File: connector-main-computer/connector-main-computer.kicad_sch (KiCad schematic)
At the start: 38 parts, among them J1 DVI-I_Dual_Link, J10 Conn_01x04_MountingPin, J11 Conn_01x04_MountingPin, J12 Conn_01x02_MountingPin, J13 Conn_01x04_MountingPin, J2 Conn_01x03_MountingPin, J3 Conn_01x03_MountingPin, J4 Conn_01x03_MountingPin, J5 Conn_01x03_MountingPin, J6 Conn_01x03_MountingPin, J7 Conn_01x04_MountingPin, J8 Conn_01x04_MountingPin, J9 Conn_01x04_MountingPin, U1 INA199xxDCK, U2 INA199xxDCK, U3 P82B96, U4 SN65HVD11HD, U5 74AHCT1G04

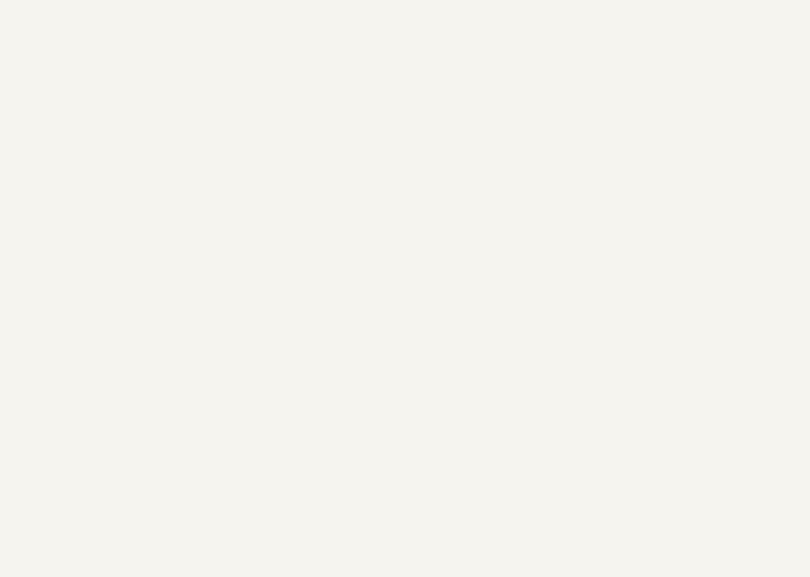
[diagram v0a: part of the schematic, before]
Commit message: Add first revision of board for main computer connector
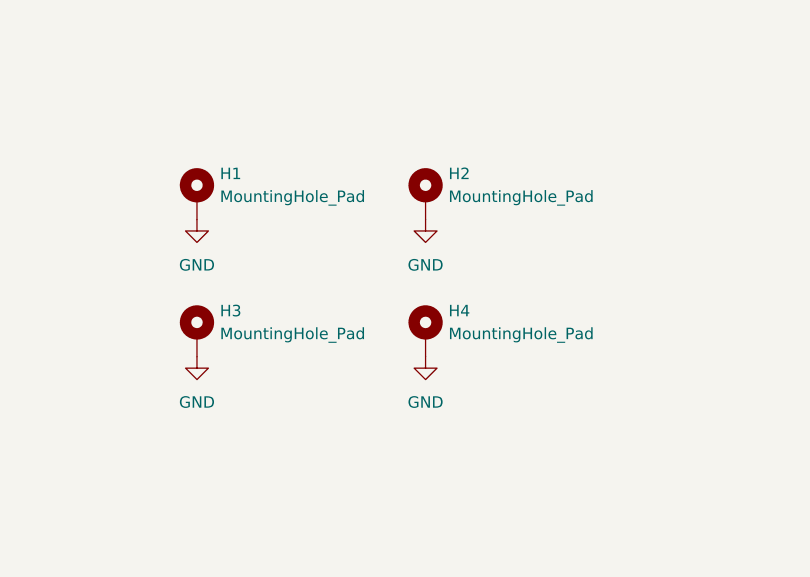
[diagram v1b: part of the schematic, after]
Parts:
- added H1, H2, H3, H4: MountingHole_Pad, MountingHole:MountingHole_3.2mm_M3_Pad_Via, symbol Mechanical:MountingHole_Pad
- C1, C2, C3, C4, C5: footprint (none) -> Capacitor_SMD:C_0805_2012Metric
- D3: footprint (none) -> Diode_SMD:D_MiniMELF
- FB1, FB2, FB3, FB4, FB5: footprint (none) -> Inductor_SMD:L_0805_2012Metric
- J1: footprint (none) -> Connector_Video:DVI-I_Molex_74320-1004_Horizontal
- J10, J11, J13, J7, J8, J9: footprint (none) -> Connector_JST:JST_PH_S4B-PH-SM4-TB_1x04-1MP_P2.00mm_Horizontal
- J12: footprint (none) -> Connector_JST:JST_PH_S2B-PH-SM4-TB_1x02-1MP_P2.00mm_Horizontal
- J2, J3, J4, J5, J6: footprint (none) -> Connector_JST:JST_PH_S3B-PH-SM4-TB_1x03-1MP_P2.00mm_Horizontal
- R1, R2, R5: footprint (none) -> Resistor_SMD:R_2512_6332Metric
- R3, R4, R6: footprint (none) -> Resistor_SMD:R_0805_2012Metric
- RV1: footprint (none) -> Potentiometer_THT:Potentiometer_Bourns_3266W_Vertical
- U3: footprint (none) -> Package_SO:SO-8_3.9x4.9mm_P1.27mm
- U5: footprint (none) -> Package_TO_SOT_SMD:SOT-23-5
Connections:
- net GND: now also H1.1, H2.1, H3.1, H4.1

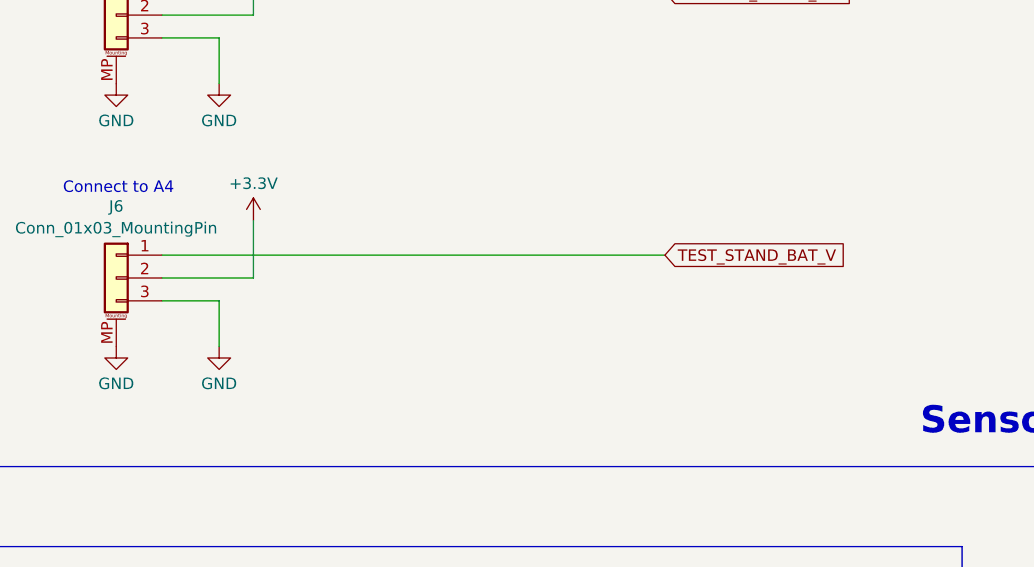
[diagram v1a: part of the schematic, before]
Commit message: add current divider
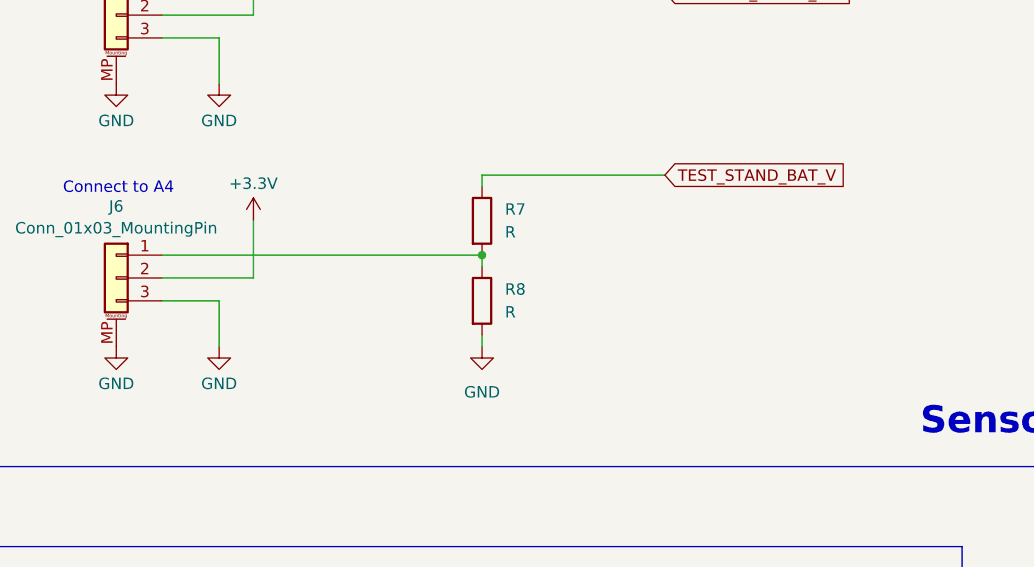
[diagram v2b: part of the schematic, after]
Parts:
- added R7, R8: R, Resistor_SMD:R_0805_2012Metric, symbol Device:R
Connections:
- net GND: now also R8.2
- net TEST_STAND_BAT_V: now also R7.1; no longer J6.1 (Pin_1)
- new net: J6.1 (Pin_1), R7.2, R8.1

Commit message: change strain power supply
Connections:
- net +12V: no longer J1.9 (D1-)
- net GND: now also J1.9 (D1-)
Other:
- note added: "FIX: Cross RX/TX and flip enable?"
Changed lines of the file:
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@@
+		)
+	)
+	(text "FIX: Cross RX/TX and flip enable?"
+		(exclude_from_sim no)
+		(at 48.514 317.246 0)
+		(effects
+			(font
+				(size 1.27 1.27)
+				(color 255 20 3 1)
+			)
 		)
 	)
@@
 	)
 	(junction
+		(at 447.04 162.56)
+		(diameter 0)
+		(color 0 0 0 0)
+	)
+	(junction
 		(at 447.04 210.82)
 		(diameter 0)
@@
 	)
 	(junction
-		(at 452.12 144.78)
-		(diameter 0)
-		(color 0 0 0 0)
-	)
-	(junction
 		(at 447.04 175.26)
 		(diameter 0)
@@
 	(wire
 		(pts
+			(xy 447.04 144.78) (xy 447.04 162.56)
+		)
+		(stroke
+			(width 0)
+			(type default)
+		)
+	)
+	(wire
+		(pts
 			(xy 445.77 160.02) (xy 463.55 160.02)
 		)
@@
 	(wire
 		(pts
-			(xy 452.12 144.78) (xy 463.55 144.78)
-		)
-		(stroke
-			(width 0)
-			(type default)
-		)
-	)
-	(wire
-		(pts
 			(xy 115.57 39.37) (xy 111.76 39.37)
 		)
@@
 	(wire
 		(pts
+			(xy 463.55 144.78) (xy 447.04 144.78)
+		)
+		(stroke
+			(width 0)
+			(type default)
+		)
+	)
+	(wire
+		(pts
 			(xy 226.06 34.29) (xy 226.06 49.53)
 		)
@@
 	(wire
 		(pts
-			(xy 452.12 139.7) (xy 452.12 144.78)
-		)
-		(stroke
-			(width 0)
-			(type default)
-		)
-	)
-	(wire
-		(pts
 			(xy 96.52 114.3) (xy 115.57 114.3)
 		)
@@
 	(wire
 		(pts
-			(xy 452.12 144.78) (xy 452.12 154.94)
-		)
-		(stroke
+			(xy 452.12 139.7) (xy 452.12 154.94)
+		)
+		(stroke

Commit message: Rework main computer connector
* Add filtering for 5V and 12V lines
* Add input protection for RS485
* Run all test stand logic on 5V - add level translation
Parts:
- added C10, C13, C14, C15, C8, C9: 100nF, Capacitor_SMD:C_0805_2012Metric, symbol Device:C
- added C11, C12: 100nF 25V, Capacitor_SMD:CP_Elec_6.3x5.8, symbol Device:C_Polarized
- added C6, C7: 100nF 16V, Capacitor_SMD:CP_Elec_6.3x5.8, symbol Device:C_Polarized
- added L1, L2: 100uH, Inductor_SMD:L_12x12mm_H8mm, symbol Device:L
- added R10, R9: 10R thick film, Resistor_SMD:R_0805_2012Metric, symbol Device:R
- added U6: CDSOT236-0504C, Package_TO_SOT_SMD:SOT-23-6, symbol Power_Protection:CDSOT236-0504C
- added U7, U8: SN74LV1T125DCK, Package_TO_SOT_SMD:SOT-353_SC-70-5, symbol Logic_LevelTranslator:SN74LV1T125DCK
- C1, C2, C4, C5: value C -> 100nF
- C3: value C -> 100nf
- D3: value D_Zener -> 3.3V Zener
- R1, R2: value R -> 0R25
- R3, R4: value R -> 330R
- R6: value R -> 10K
- R7: value R -> 1K
- R8: value R -> 14K
- RV1: value R_Potentiometer -> 47K
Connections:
- net +12V: now also C12.1, C13.1, L2.2; no longer C3.1, J1.15 (GND), J1.C4 (HSYNC), J10.3 (Pin_3), J11.3 (Pin_3), J13.3 (Pin_3), R3.1, R4.1, U3.8 (VCC)
- net +3.3V: now also C14.1, U7.5 (VCC); no longer C4.1, J1.14 (+5V), J1.18 (D0+), J1.C2 (Green), U4.8 (VCC)
- net GND: now also C10.2, C11.2, C12.2, C13.2, C14.2, C15.2, C6.2, C7.2, C8.2, C9.2, U6.2 (VN), U7.1 (~{OE}), U7.3 (GND), U8.1 (~{OE}), U8.3 (GND)
- net RS485 bus A: now also R9.2, U6.1 (IO1), U6.6 (IO4); no longer R5.1, U4.7 (B)
- net RS485 bus B: now also R10.2, U6.3 (IO2), U6.4 (IO3); no longer R5.2, U4.6 (A)
- net RX: now also U7.2 (A); no longer J9.3 (Pin_3)
- net TX: now also U8.4 (Y); no longer J9.4 (Pin_4)
- net at J7.2 (Pin_2), J8.2 (Pin_2), J9.2 (Pin_2): now also C6.1, C8.1, L1.1
- new net: J9.3 (Pin_3), U7.4 (Y)
- new net: R10.1, R5.2, U4.6 (A)
- new net: R5.1, R9.1, U4.7 (B)
- new net: J9.4 (Pin_4), U8.2 (A)
- new net +5V: C15.1, C3.1, C4.1, C7.1, C9.1, J1.14 (+5V), J1.15 (GND), J1.18 (D0+), J1.C2 (Green), J1.C4 (HSYNC), L1.2, R3.1, R4.1, U3.8 (VCC), U4.8 (VCC), U6.5 (VP), U8.5 (VCC)
- new net VDD: C10.1, C11.1, J10.3 (Pin_3), J11.3 (Pin_3), J13.3 (Pin_3), L2.1
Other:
- note added: "3.3V <=> 5V translator"
- note added: "Use INA210, same pinout just available on tme.eu"
- note added: "Use SN65HVD485, same pinout just available on tme.eu"
- note removed: "FIX: Cross RX/TX and flip enable?"
- moved on the sheet: C5, D3, H1, H2, H3, H4, J12, J13, R6, U5

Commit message: updates
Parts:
- R7: value 1K -> 13,7k
- R8: value 14K -> 1K
- U1: value INA199xxDCK -> INA210
- U4: value SN65HVD11HD -> SN65HVD485E
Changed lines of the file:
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@@
 			)
 		)
-		(property "Value" "1K"
+		(property "Value" "13,7k"
 			(at 97.79 177.7999 0)
 			(effects
@@
 		(fields_autoplaced yes)
 		(property "Reference" "U4"
-			(at 97.3933 307.0055 0)
+			(at 97.3933 306.07 0)
 			(effects
 				(font
@@
 			)
 		)
-		(property "Value" "SN65HVD11HD"
-			(at 97.3933 309.4298 0)
+		(property "Value" "SN65HVD485E"
+			(at 97.3933 308.61 0)
 			(effects
 				(font
@@
 		(fields_autoplaced yes)
 		(property "Reference" "U1"
-			(at 97.0981 37.7655 0)
+			(at 97.0981 36.83 0)
 			(effects
 				(font
@@
 			)
 		)
-		(property "Value" "INA199xxDCK"
-			(at 97.0981 40.1898 0)
+		(property "Value" "INA210"
+			(at 97.0981 39.37 0)
 			(effects
 				(font
@@
 			)
 		)
-		(property "Value" "14K"
+		(property "Value" "1K"
 			(at 97.79 186.6899 0)
 			(effects
